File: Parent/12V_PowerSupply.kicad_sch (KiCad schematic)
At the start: 1 part, among them U10 LM3480-12

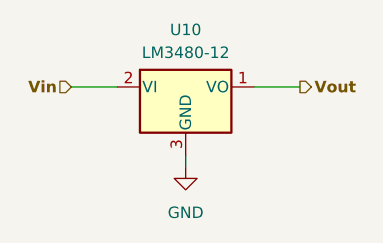
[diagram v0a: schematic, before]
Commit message: Updated Parent - Moved workspace to cloud
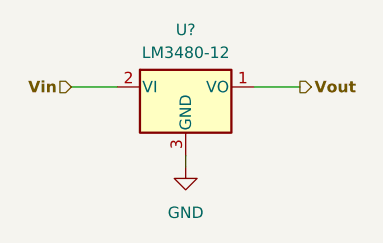
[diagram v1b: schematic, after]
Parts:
- renumbered U10 to U?
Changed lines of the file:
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@@
   (symbol (lib_id "power:GND") (at 144.78 71.12 0) (unit 1)
     (in_bom yes) (on_board yes) (dnp no) (fields_autoplaced)
-    (property "Reference" "#PWR030" (at 144.78 77.47 0)
+    (property "Reference" "#PWR?" (at 144.78 77.47 0)
       (effects (font (size 1.27 1.27)) hide)
     )
@@
       (project "Parent"
         (path "/1451ec1d-c665-471b-ba41-1d89ef6a63bf/7708e5b2-0a75-40c8-a3d2-8281cd192259"
-          (reference "#PWR030") (unit 1)
+          (reference "#PWR?") (unit 1)
         )
       )
@@
   (symbol (lib_id "Regulator_Linear:LM3480-12") (at 144.78 62.23 0) (unit 1)
     (in_bom yes) (on_board yes) (dnp no) (fields_autoplaced)
-    (property "Reference" "U10" (at 144.78 55.88 0)
+    (property "Reference" "U?" (at 144.78 55.88 0)
       (effects (font (size 1.27 1.27)))
     )
@@
       (project "Parent"
         (path "/1451ec1d-c665-471b-ba41-1d89ef6a63bf/7708e5b2-0a75-40c8-a3d2-8281cd192259"
-          (reference "U10") (unit 1)
+          (reference "U?") (unit 1)
         )
       )
